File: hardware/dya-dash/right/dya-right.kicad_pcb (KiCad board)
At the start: 2 copper layers, 127.2 x 92.9 mm, 123 parts

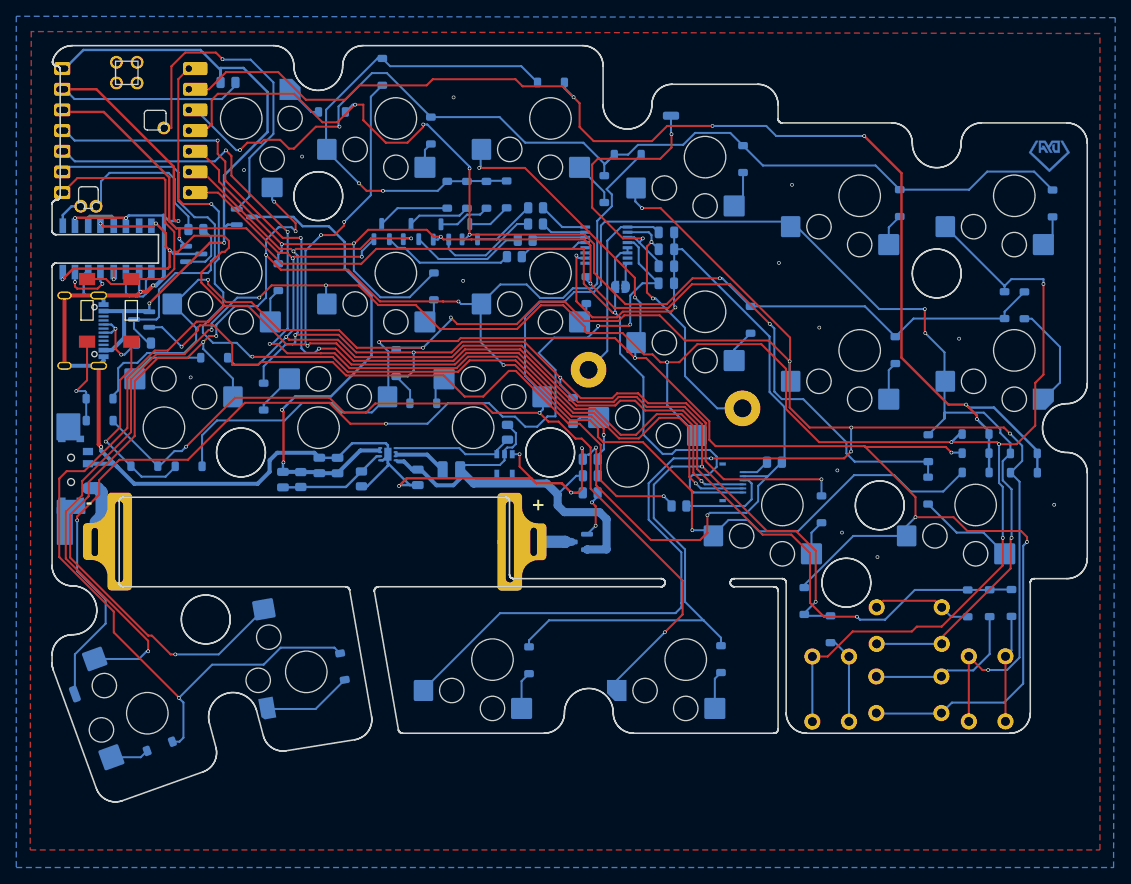
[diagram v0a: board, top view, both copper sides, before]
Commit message: Change FFC connector direction for arrow model
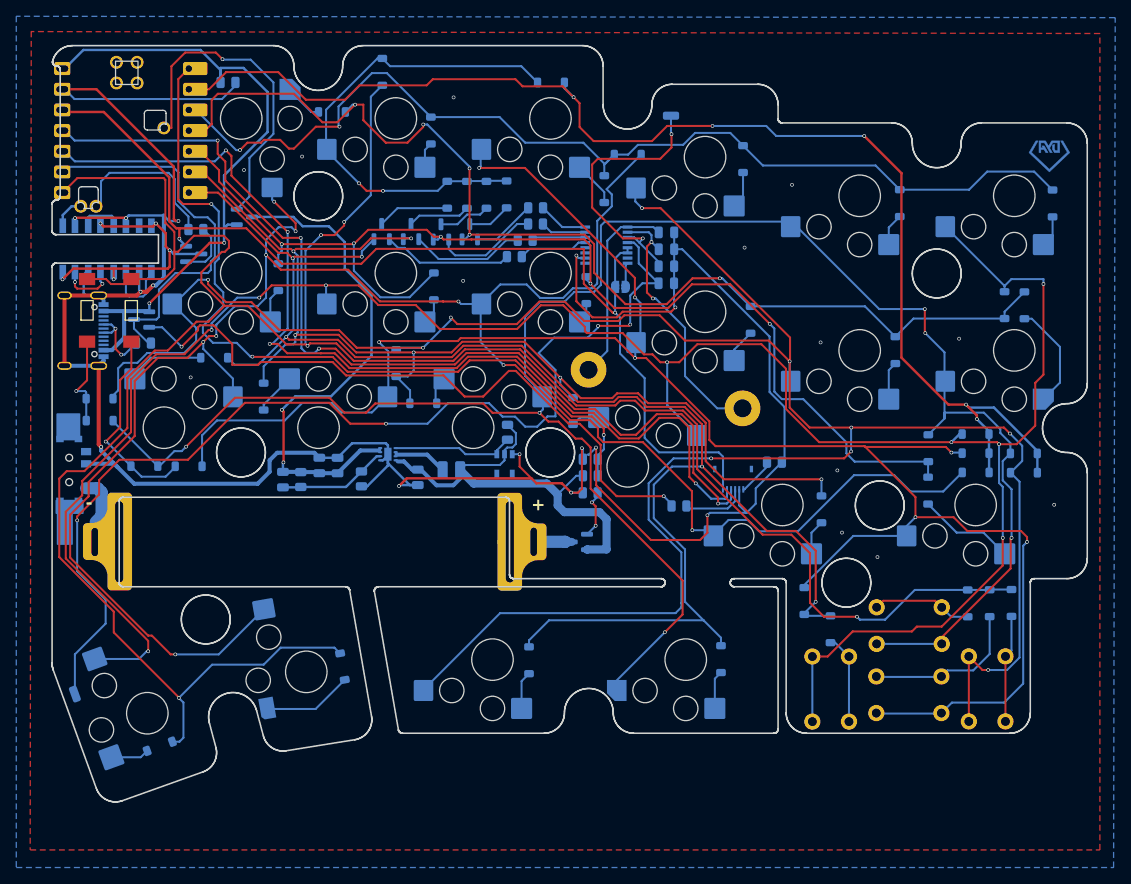
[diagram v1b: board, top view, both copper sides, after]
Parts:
- moved JR3 1.49 mm to (105.5, 72.7), turned to 0 degrees
- moved SW_BATR1 0.23 mm to (23.9, 70.3)
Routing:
- net 3.3V_R: track 136.9 -> 128.3 mm
- net MOTION_R: track 11.5 -> 7.93 mm
- net SDIO_R: track 118.6 -> 120.0 mm
- net Net-(JR3-Pin_6): track 3.46 -> 4.63 mm
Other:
- outline, holes or cut-outs redrawn
- board text added: "DYA Dash Rev2.2"
- board text removed: "DYA Dash Rev2.0"
